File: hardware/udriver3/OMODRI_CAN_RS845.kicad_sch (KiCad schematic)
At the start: 12 parts, among them J13 conn_01x02_MountingPins, U17 TCAN330G, U18 THVD24x0

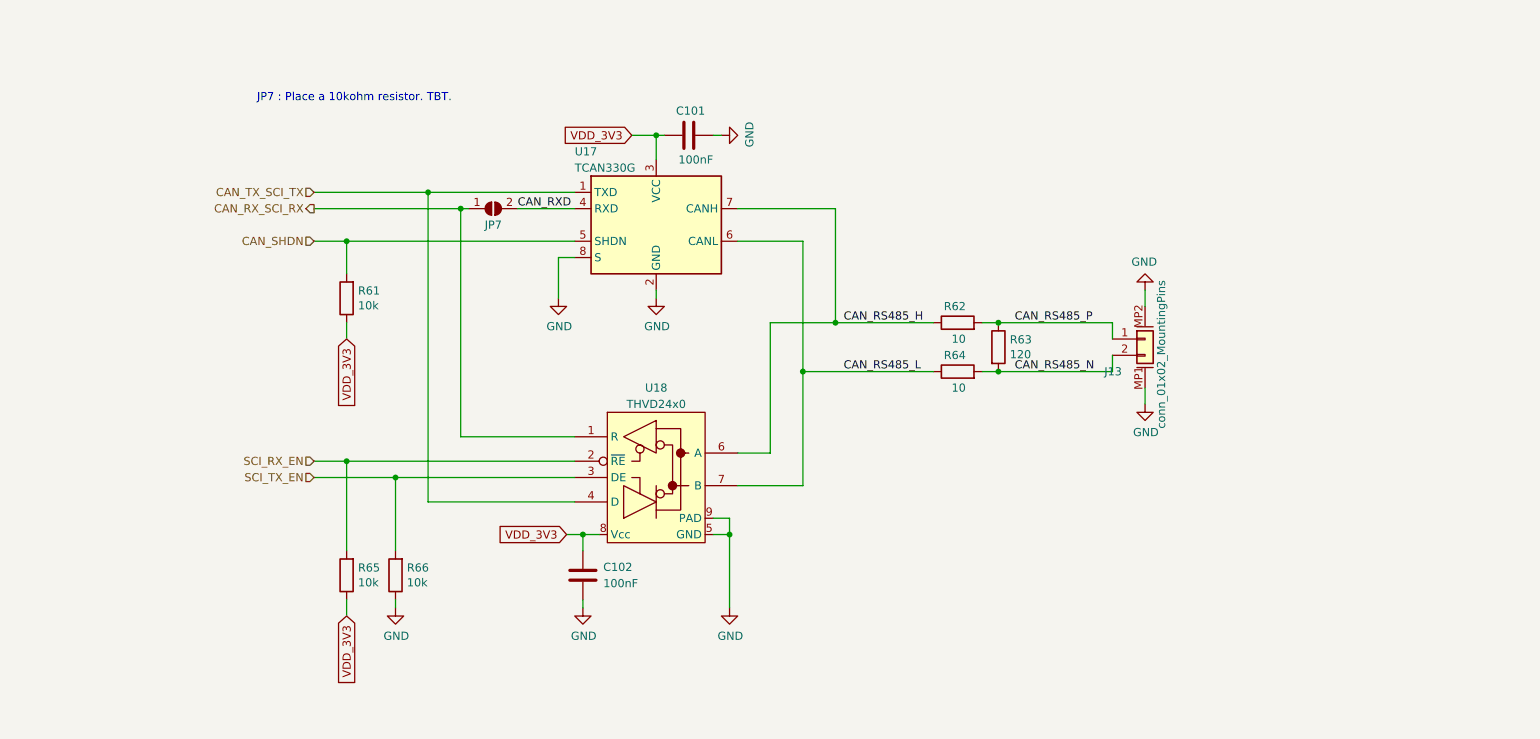
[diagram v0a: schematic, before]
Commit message: First release of uOmodri v3. Swap COM SPI. Modify CAN to CAN FD and bus sharing with RS485.
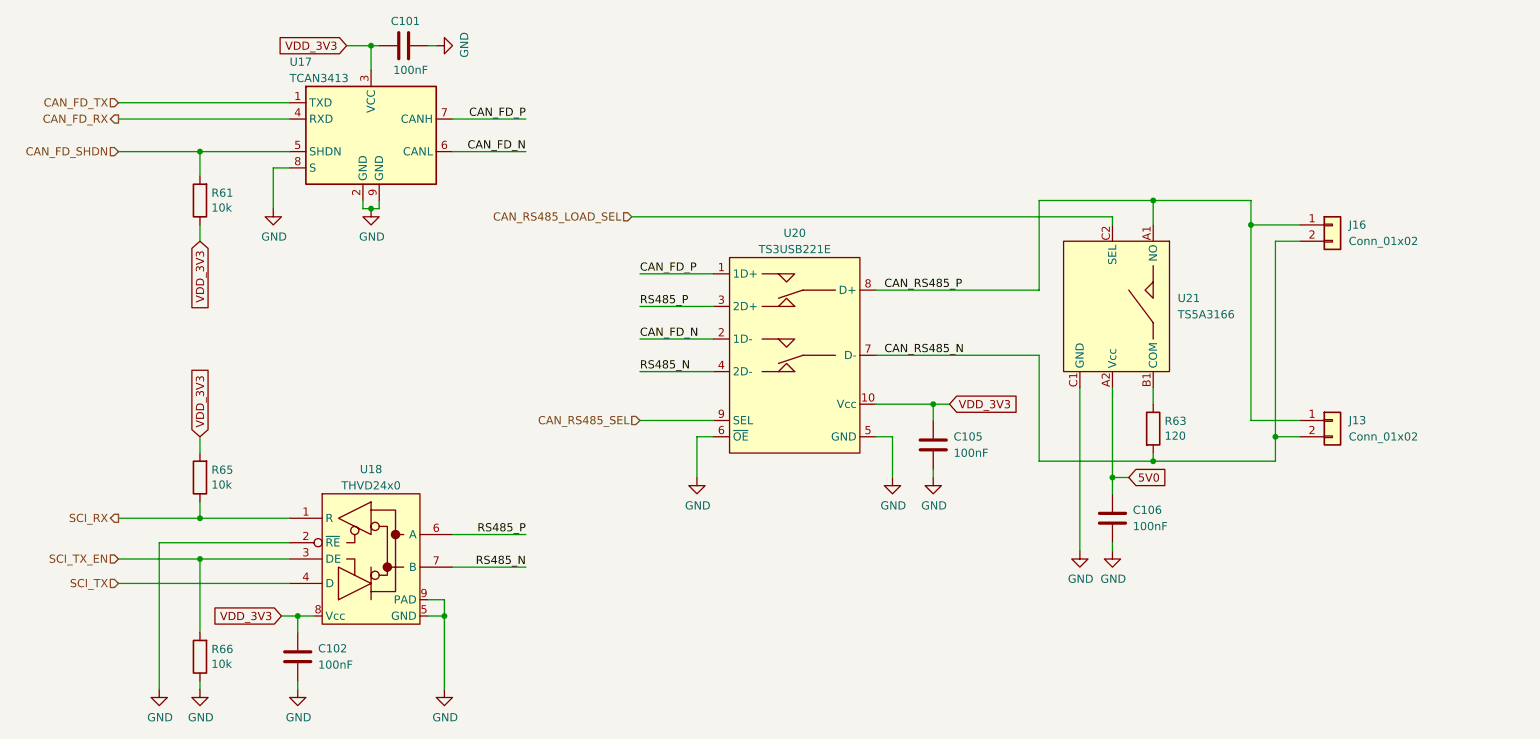
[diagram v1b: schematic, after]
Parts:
- removed J13: conn_01x02_MountingPins, udriver3:Hirose_DF13_02P-1.25H_1x02_P1.25mm_Right_angle, symbol omodri_lib:conn_01x02_MountingPins
- removed JP7: SolderJumper_2_Open, Jumper:SolderJumper-2_P1.3mm_Open_Pad1.0x1.5mm, symbol Jumper:SolderJumper_2_Open
- removed R62, R64: 10, Resistor_SMD:R_0201_0603Metric, symbol Device:R
- removed U17: TCAN330G, Package_TO_SOT_SMD:TSOT-23-8, symbol Interface_CAN_LIN:TCAN330G
- added C105, C106: 100nF, Capacitor_SMD:C_0201_0603Metric, symbol Device:C
- added J13, J16: Conn_01x02, udriver3:Hirose_DF13-02P-1.25DS_1x02_P1.25mm_Horizontal, symbol Connector_Generic:Conn_01x02
- added U17: TCAN3413, udriver3:VSON-8-1EP_3.0x3.0mm_P0.65mm_EP1.65x2.4mm, symbol omodri_lib:TCAN3413
- added U20: TS3USB221E, udriver3:UQFN-10_1.5x2mm_P0.5mm, symbol omodri_lib:TS3USB221
- added U21: TS5A3166, udriver3:DSBGA-5_0.888x1.388mm_P0.5mm, symbol omodri_lib:TS5A3166
- R63: footprint Resistor_THT:R_Axial_DIN0204_L3.6mm_D1.6mm_P5.08mm_Horizontal -> Resistor_SMD:R_0201_0603Metric; DigiKey P122692CT-ND -> (none); Farnell 2396857 -> (none)
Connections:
- net CAN_RS485_N: now also J13.2 (Pin_2), J16.2 (Pin_2), U20.7 (D-)
- net CAN_RS485_P: now also J13.1 (Pin_1), J16.1 (Pin_1), U20.8 (D+), U21.A1 (NO); no longer R63.1
- net GND: now also U18.2 (~{RE}), C105.2, C106.2, U17.2 (GND), U17.8 (S), U17.9 (GND), U20.5 (GND), U20.6 (~{OE}), U21.C1 (GND)
- net VDD_3V3: now also R65.2, C105.1, U17.3 (VCC), U20.10 (Vcc); no longer R65.1
- net CAN_RS485_H renamed RS485_P
- net RS485_P: now also U20.3 (2D+)
- net CAN_RS485_L renamed RS485_N
- net RS485_N: now also U20.4 (2D-)
- net CAN_RX_SCI_RX renamed SCI_RX
- net SCI_RX: now also R65.1
- net CAN_SHDN renamed CAN_FD_SHDN
- net CAN_FD_SHDN: now also U17.5 (SHDN)
- net CAN_TX_SCI_TX renamed SCI_TX
- removed net SCI_RX_EN: R65.2, U18.2 (~{RE})
- new net: R63.1, U21.B1 (COM)
- new net 5V0: C106.1, U21.A2 (Vcc)
- new net CAN_FD_N: U17.6 (CANL), U20.2 (1D-)
- new net CAN_FD_P: U17.7 (CANH), U20.1 (1D+)
- new net CAN_FD_RX: U17.4 (RXD)
- new net CAN_FD_TX: U17.1 (TXD)
- new net CAN_RS485_LOAD_SEL: U21.C2 (SEL)
- new net CAN_RS485_SEL: U20.9 (SEL)
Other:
- note removed: "JP7 : Place a 10kohm resistor. TBT."
- moved on the sheet: C101, C102, R61, R63, R66, U18

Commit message: Modify JP5/JP6 jumper to remove DRC error. Add gate resistor on power MOSFET (high & low side).
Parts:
- removed J13, J16: Conn_01x02, udriver3:Hirose_DF13-02P-1.25DS_1x02_P1.25mm_Horizontal, symbol Connector_Generic:Conn_01x02
- removed U21: TS5A3166, udriver3:DSBGA-5_0.888x1.388mm_P0.5mm, symbol omodri_lib:TS5A3166
- added J13: conn_01x02_MountingPins, udriver3:Hirose_DF13_02P-1.25H_1x02_P1.25mm_Right_angle, symbol omodri_lib:conn_01x02_MountingPins
- added U21: TS5A3166D, Package_TO_SOT_SMD:SOT-353_SC-70-5, symbol omodri_lib:TS5A3166_SOT
- U17: Mouser (none) -> 595-PTCAN3413DRBR; Part No (none) -> PTCAN3413DRBR
- U20: DigiKey (none) -> 296-25222-1-ND; Farnell (none) -> 3124910; Mouser (none) -> 595-TS3USB221ERSER; Part No (none) -> TS3USB221ERSER; RS (none) -> 817-5575
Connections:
- net 5V0: now also U21.5 (Vcc)
- net CAN_RS485_LOAD_SEL: now also U21.4 (SEL)
- net CAN_RS485_N: now also J13.1 (Pin_1)
- net CAN_RS485_P: now also J13.2 (Pin_2), U21.1 (NO)
- net GND: now also J13.MP1 (MountPin1), J13.MP2 (MountPin2), U21.3 (GND)
- net at R63.1: now also U21.2 (COM)

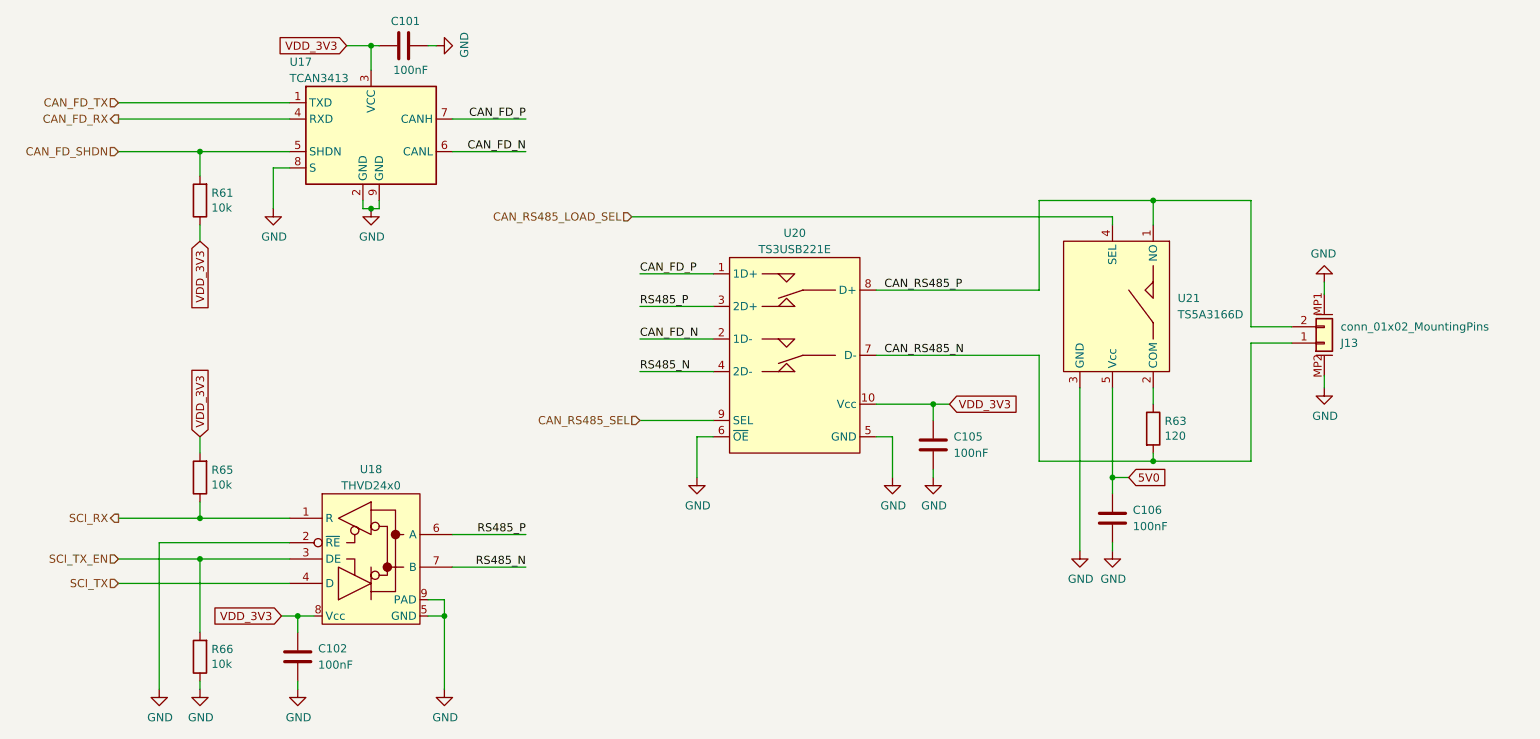
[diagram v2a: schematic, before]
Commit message: Update of the load connect/disconnect on the CAN/RS485 bus. Remove the electronic switch replaced by a 1.27mm jumper.
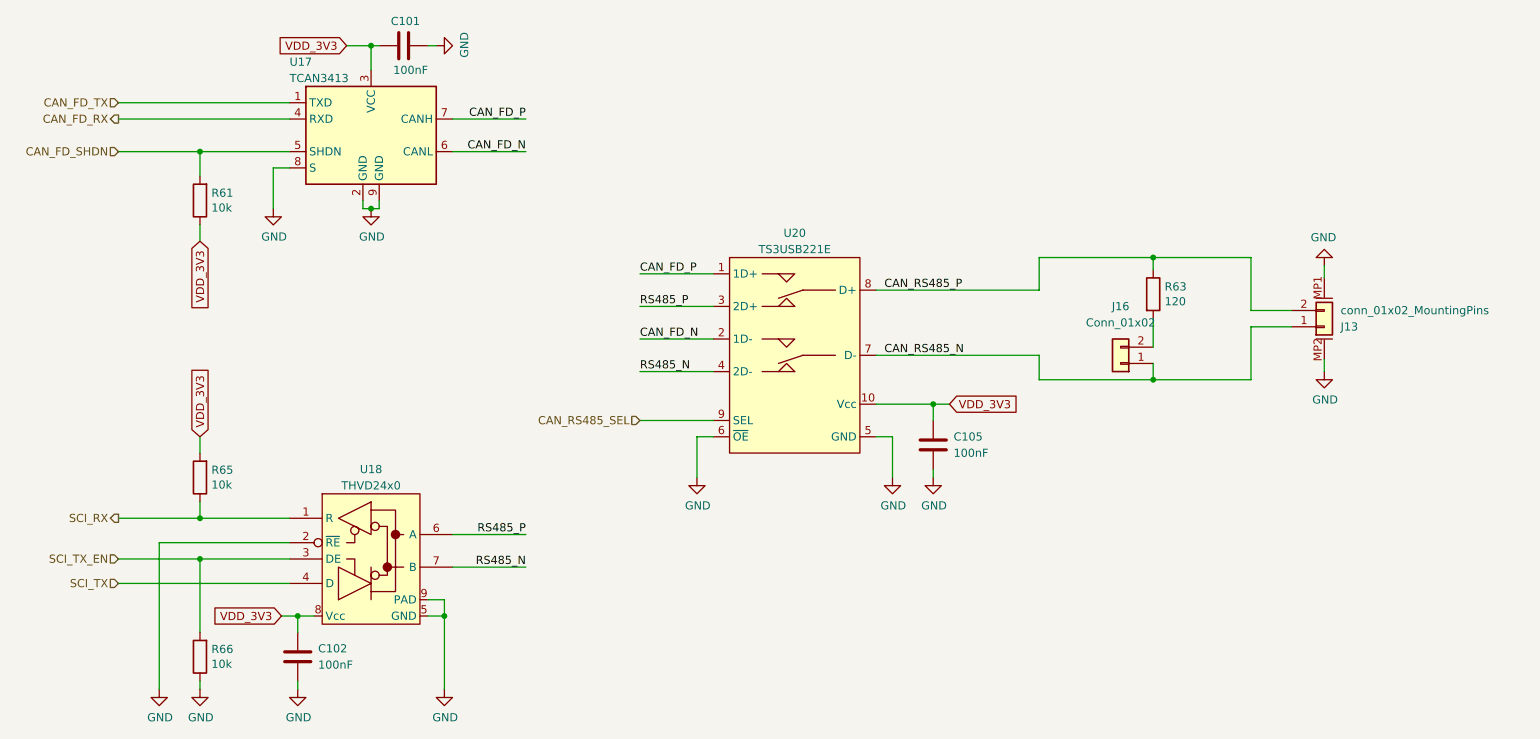
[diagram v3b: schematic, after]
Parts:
- removed C106: 100nF, Capacitor_SMD:C_0201_0603Metric, symbol Device:C
- removed U21: TS5A3166D, Package_TO_SOT_SMD:SOT-353_SC-70-5, symbol omodri_lib:TS5A3166_SOT
- added J16: Conn_01x02, Connector_PinHeader_1.27mm:PinHeader_1x02_P1.27mm_Vertical, symbol Connector_Generic:Conn_01x02
- J13: DigiKey (none) -> H126390-ND; Mouser (none) -> 798-DF13-2P-1.25H76; Part No (none) -> DF13-2P-1.25H(76); RS (none) -> 188-6440
- R63: DigiKey (none) -> P122692CT-ND; Farnell (none) -> 2396857
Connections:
- net CAN_RS485_N: now also J16.1 (Pin_1); no longer R63.2
- net CAN_RS485_P: now also R63.1
- new net: J16.2 (Pin_2), R63.2
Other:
- moved on the sheet: J13, R63

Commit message: Add JLCPCB components ref where it was matching.
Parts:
- C101, C102, C105: LCSC (none) -> C2649540
- J13: LCSC (none) -> C597868
- R61, R65, R66: LCSC (none) -> C9900024792
- U18: LCSC (none) -> C2878080
- U20: LCSC (none) -> C129313
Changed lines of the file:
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@@
+      (effects (font (size 1.27 1.27)) hide)
+    )
+    (property "LCSC" "C9900024792" (at 73.66 144.78 0)
       (effects (font (size 1.27 1.27)) hide)
     )
@@
     )
     (property "RS" "817-5575" (at 166.37 92.71 0)
+      (effects (font (size 1.27 1.27)) hide)
+    )
+    (property "LCSC" "C129313" (at 166.37 92.71 0)
       (effects (font (size 1.27 1.27)) hide)
     )
@@
       (effects (font (size 1.27 1.27)) hide)
     )
+    (property "LCSC" "C9900024792" (at 73.66 116.84 0)
+      (effects (font (size 1.27 1.27)) hide)
+    )
     (pin "1")
     (pin "2")
@@
     )
     (property "Part No" "THVD2450DRBR" (at 100.33 128.27 0)
+      (effects (font (size 1.27 1.27)) hide)
+    )
+    (property "LCSC" "C2878080" (at 100.33 128.27 0)
       (effects (font (size 1.27 1.27)) hide)
     )
@@
       (effects (font (size 1.27 1.27)) hide)
     )
+    (property "LCSC" "" (at 100.33 63.5 0)
+      (effects (font (size 1.27 1.27)) hide)
+    )
     (pin "3")
     (pin "4")
@@
       (effects (font (size 1.27 1.27)) hide)
     )
+    (property "LCSC" "C2649540" (at 88.9 144.78 0)
+      (effects (font (size 1.27 1.27)) hide)
+    )
     (pin "1")
     (pin "2")
@@
       (effects (font (size 1.27 1.27)) hide)
     )
+    (property "LCSC" "C2649540" (at 105.41 49.53 0)
+      (effects (font (size 1.27 1.27)) hide)
+    )
     (pin "1")
     (pin "2")
@@
     )
     (property "Rated Voltage" "25V" (at 187.96 111.76 0)
+      (effects (font (size 1.27 1.27)) hide)
+    )
+    (property "LCSC" "C2649540" (at 187.96 111.76 0)
       (effects (font (size 1.27 1.27)) hide)
     )
@@
     )
     (property "RS" "176-3597" (at 73.66 73.66 0)
+      (effects (font (size 1.27 1.27)) hide)
+    )
+    (property "LCSC" "C9900024792" (at 73.66 73.66 0)
       (effects (font (size 1.27 1.27)) hide)
     )
@@
       (effects (font (size 1.27 1.27)) hide)
     )
+    (property "LCSC" "" (at 217.17 99.06 0)
+      (effects (font (size 1.27 1.27)) hide)
+    )
     (pin "2")
     (pin "1")
@@
       (effects (font (size 1.27 1.27)) hide)
     )
+    (property "LCSC" "C597868" (at 248.92 92.075 0)
+      (effects (font (size 1.27 1.27)) hide)
+    )
     (pin "MP2")
     (pin "1")
@@
       (effects (font (size 1.27 1.27)) hide)
     )
+    (property "LCSC" "" (at 222.25 88.265 0)
+      (effects (font (size 1.27 1.27)) hide)
+    )

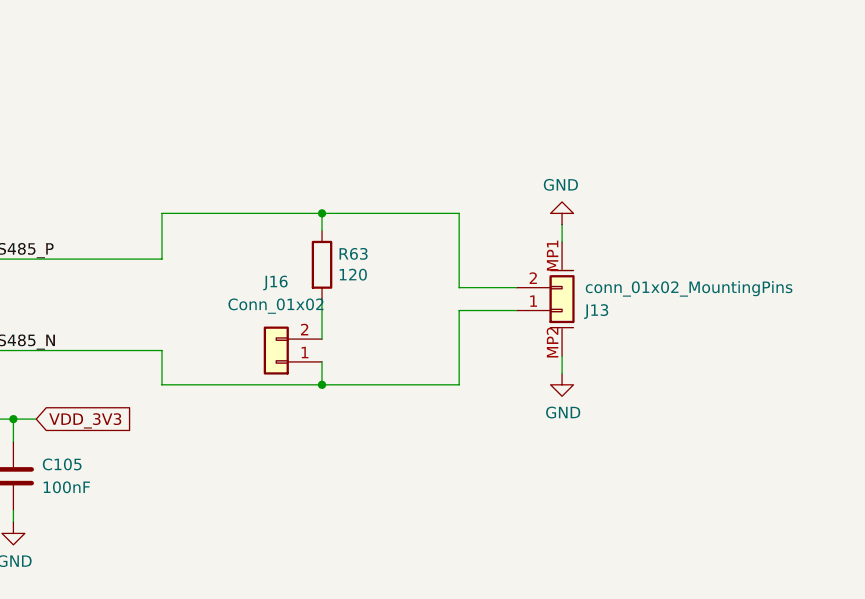
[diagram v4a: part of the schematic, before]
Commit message: Update PCB layout to match JLCPCB requirements (via diameter). Set Netclass constraints defined in uOmodri_v2.
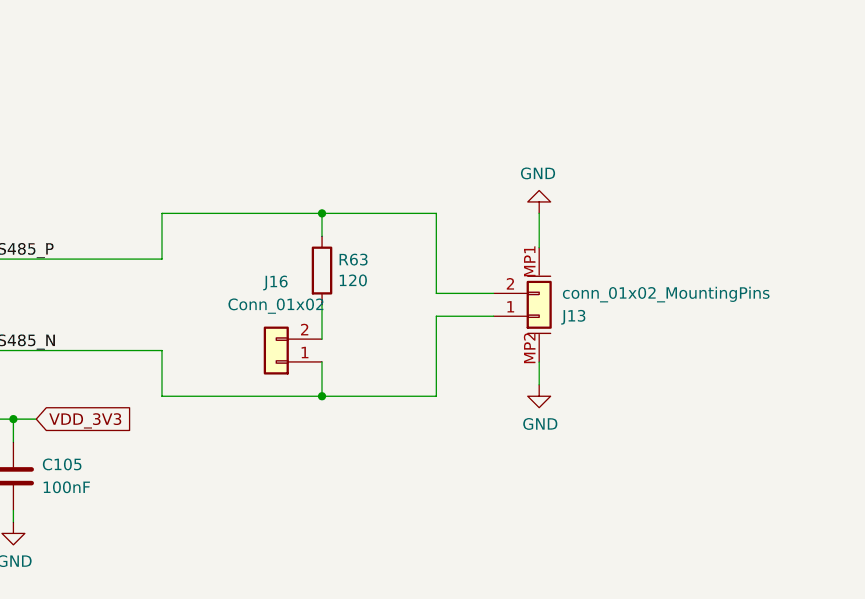
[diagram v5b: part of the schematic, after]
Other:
- moved on the sheet: J13, R63
